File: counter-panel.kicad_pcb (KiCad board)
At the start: 2 copper layers, 60.6 x 133.4 mm, 13 parts

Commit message: Rev. 2
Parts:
- moved REF** 4.90 mm to (124.6, 160.4)
- moved REF** 4.90 mm to (78.6, 160.4)
- moved REF** 4.90 mm to (85.1, 122.2)
- moved REF** 4.90 mm to (101.6, 122.2)
- moved REF** 4.90 mm to (118.1, 122.2)
- moved REF** 4.90 mm to (101.6, 155.0)
- moved REF** 4.90 mm to (101.6, 138.7)
- moved REF** 4.90 mm to (118.1, 138.7)
- moved REF** 4.90 mm to (85.1, 138.7)
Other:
- board size 60.6 x 133.4 mm -> 60.6 x 128.5 mm
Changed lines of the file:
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@@
 	(footprint "MAI_PanelHole:PanelHole_D6Rxx"
 		(layer "F.Cu")
-		(at 118.11 127.095)
+		(at 118.11 122.195)
 		(property "Reference" "REF**"
 			(at 0 -0.5 0)
@@
 		)
 		(attr board_only exclude_from_pos_files exclude_from_bom allow_missing_courtyard)
+		(fp_rect
+			(start -5.65 -6.25)
+			(end 6.25 6.25)
+			(stroke
+				(width 0.05)
+				(type solid)
+			)
+			(fill no)
+			(layer "F.CrtYd")
+		)
 		(fp_text user "${REFERENCE}"
 			(at 0 2.5 0)
@@
 	(footprint "MAI_PanelHole:PanelHole_PJ301BM"
 		(layer "F.Cu")
-		(at 101.6 143.605)
+		(at 101.6 138.705)
 		(property "Reference" "REF**"
 			(at 0 -0.5 0)
@@
 		)
 		(attr board_only exclude_from_pos_files exclude_from_bom allow_missing_courtyard)
+		(fp_rect
+			(start -5.4 -6.2)
+			(end 5.4 5.7)
+			(stroke
+				(width 0.05)
+				(type solid)
+			)
+			(fill no)
+			(layer "F.CrtYd")
+		)
 		(fp_text user "${REFERENCE}"
 			(at 0 2.5 0)
@@
 	(footprint "MAI_Logo:MAI_Logo_10.5mm_Soldermask"
 		(layer "F.Cu")
-		(at 101.6 159.865)
+		(at 101.6 154.965)
 		(property "Reference" "REF**"
 			(at 0 -0.5 0)
@@
 		)
 		(group ""
-			(members "007e59d5-dd87-4414-bfcb-8a791d01e0a8" "5d55bc7f-9524-44fe-8a44-d4192dc5d49f"
-				"ee19ec08-60ec-448d-a128-6061143b3cac"
+			(members "304329a8-93d0-4710-89da-b5f9ca749a7c" "a1dcff84-941b-45ea-a03c-113b23a4899f"
+				"ed1a71e2-07de-497b-ab26-7d1f4ce3553c"
 			)
 		)
@@
 		)
 		(fp_rect
+			(start -2.13 -2.54)
+			(end 17.37 35.56)
+			(stroke
+				(width 0.05)
+				(type solid)
+			)
+			(fill no)
+			(layer "F.CrtYd")
+		)
+		(fp_rect
 			(start 17.12 -2.29)
 			(end -1.88 35.31)
@@
 		)
 		(group ""
-			(members "0314770b-07c4-4799-91cd-ce2d32d9cd09" "46357c1f-7430-4531-8edb-69de8b4cd5fb"
-				"46f7f278-1ce7-49fd-b8e8-32372eb0f30b" "94e10fc9-aa04-4488-8e95-dc1f43b66b6a"
-				"ae31dfa5-9d65-4859-966f-7c5d5160bc3b" "beac1812-f0e9-4054-995f-46d35df900fc"
-				"d999300a-5dc8-4ff8-9753-1f82308b7aea" "df0ef669-530f-4ded-bc9d-675b1c817072"
-				"ebd1850c-bc41-46ad-b8f3-3c44abb019f9"
+			(members "164f0c18-09da-4f02-918c-8de093eaadf8" "17211ef4-0c99-49b5-9bb5-683393077b98"
+				"4afb6f95-e186-4992-9f95-601ac5eb0ac2" "5722b74d-b866-46bd-bd4b-224809068712"
+				"9e1bc70c-4c6f-4915-9856-34eb29197225" "b5a80484-6aaa-4b5e-95ee-2f22a0b5214f"
+				"d0f61f16-cb09-4da3-8dd0-288c4137002b" "d6363b40-4efe-4ee9-a46f-7f5150fb9bf6"
+				"f8c60605-8abd-44bd-bc4b-592a4be05baf"
 			)
 		)
@@
 		)
 		(fp_rect
+			(start -2.13 -2.54)
+			(end 17.37 35.56)
+			(stroke
+				(width 0.05)
+				(type solid)
+			)
+			(fill no)
+			(layer "F.CrtYd")
+		)
+		(fp_rect
 			(start 17.12 -2.29)
 			(end -1.88 35.31)
@@
 		)
 		(group ""
-			(members "0718e5cc-82fb-4867-9d9d-0d31b20be6ac" "0e933451-6ab9-45d7-987d-553bd9a59f48"
-				"39c4f329-30bf-48c5-a186-0e9d4045573b" "40285d72-560b-40a3-becc-59d6b23297b2"
-				"b9054f5f-2db8-4309-b650-e811e8badf08" "be7256dd-f8c9-4556-b094-f6eccc31749b"
-				"c52d14fc-486d-475e-a465-ecf5a4b59eef" "d59265ac-db7d-4d4c-b0e9-78b0ffbd3e86"
-				"f33d80c7-e85c-4af6-96c6-dfac4c1676c2"
+			(members "1924449c-67cb-467a-8796-df98bb2279b6" "3a6cdd18-6018-436c-90c4-f8c9ebc832d7"
+				"4e4a7a91-d7b2-4769-9c2f-26a616b300c3" "72f5ae3b-22af-406f-b730-0e4100dc7158"
+				"c9e218e7-14f0-4782-8d70-630dd5abf210" "d5b6e767-6c86-4224-b7d1-8c03cd33c635"
+				"e360bcd1-de0b-4e42-83ec-22f8f9767f02" "ea660fa0-5717-46c5-b4be-eabed19c45d7"
+				"f14bb1ab-4958-4e47-bdb4-c58802fefbf7"
 			)
 		)
@@
 	(footprint "MAI_PanelHole:PanelHole_D6Rxx"
 		(layer "F.Cu")
-		(at 118.11 143.605)
+		(at 118.11 138.705)
 		(property "Reference" "REF**"
 			(at 0 -0.5 0)
@@
 		)
 		(attr board_only exclude_from_pos_files exclude_from_bom allow_missing_courtyard)
+		(fp_rect
+			(start -5.65 -6.25)
+			(end 6.25 6.25)
+			(stroke
+				(width 0.05)
+				(type solid)
+			)
+			(fill no)
+			(layer "F.CrtYd")
+		)
 		(fp_text user "${REFERENCE}"
 			(at 0 2.5 0)
@@
 	(footprint "MAI_PanelHole:PanelHole_PJ301BM"
 		(layer "F.Cu")
-		(at 85.09 143.605)
+		(at 85.09 138.705)
 		(property "Reference" "REF**"
 			(at 0 -0.5 0)
@@
 		)
 		(attr board_only exclude_from_pos_files exclude_from_bom allow_missing_courtyard)
+		(fp_rect
+			(start -5.4 -6.2)
+			(end 5.4 5.7)
+			(stroke
+				(width 0.05)
+				(type solid)
+			)
+			(fill no)
+			(layer "F.CrtYd")
+		)
 		(fp_text user "${REFERENCE}"
 			(at 0 2.5 0)
@@
 	(footprint "MAI_PanelHole:PanelHole_EurorackMounting"
 		(layer "F.Cu")
-		(at 124.64 165.3)
+		(at 124.64 160.4)
 		(property "Reference" "REF**"
 			(at 0 -0.5 0)
@@
 	(footprint "MAI_PanelHole:PanelHole_EurorackMounting"
 		(layer "F.Cu")
-		(at 78.56 165.3)
+		(at 78.56 160.4)
 		(property "Reference" "REF**"
 			(at 0 -0.5 0)
@@
 	(footprint "MAI_PanelHole:PanelHole_PJ301BM"
 		(layer "F.Cu")
-		(at 85.09 127.095)
+		(at 85.09 122.195)
 		(property "Reference" "REF**"
 			(at 0 -0.5 0)
@@
 		)
 		(attr board_only exclude_from_pos_files exclude_from_bom allow_missing_courtyard)
+		(fp_rect
+			(start -5.4 -6.2)
+			(end 5.4 5.7)
+			(stroke
+				(width 0.05)
+				(type solid)
+			)
+			(fill no)
+			(layer "F.CrtYd")
+		)
 		(fp_text user "${REFERENCE}"
 			(at 0 2.5 0)
@@
 	(footprint "MAI_PanelHole:PanelHole_PJ301BM"
 		(layer "F.Cu")
-		(at 101.6 127.095)
+		(at 101.6 122.195)
 		(property "Reference" "REF**"
 			(at 0 -0.5 0)
@@
 		)
 		(attr board_only exclude_from_pos_files exclude_from_bom allow_missing_courtyard)
+		(fp_rect
+			(start -5.4 -6.2)
+			(end 5.4 5.7)
+			(stroke
+				(width 0.05)
+				(type solid)
+			)
+			(fill no)
+			(layer "F.CrtYd")
+		)
 		(fp_text user "${REFERENCE}"
 			(at 0 2.5 0)
@@
 	)
 	(gr_line
-		(start 90.14 143.605)
-		(end 96.52 143.605)
+		(start 85.09 127.275)
+		(end 85.09 133.625)
+		(stroke
+			(width 0.25)
+			(type solid)
+		)
+		(layer "F.Mask")
+	)
+	(gr_line
+		(start 85.09 133.6675)
+		(end 84.455 133.0325)
+		(stroke
+			(width 0.25)
+			(type solid)
+		)
+		(layer "F.Mask")
+	)
+	(gr_line
+		(start 85.09 133.6675)
+		(end 85.725 133.0325)
+		(stroke
+			(width 0.25)
+			(type solid)
+		)
+		(layer "F.Mask")
+	)
+	(gr_line
+		(start 90.14 122.195)
+		(end 96.52 122.195)
 		(stroke
 			(width 0.25)
@@
 	)
 	(gr_line
-		(start 106.68 127.095)
-		(end 111.76 127.095)
+		(start 90.14 138.705)
+		(end 96.52 138.705)
+		(stroke
+			(width 0.25)
+			(type dash_dot_dot)
+		)
+		(layer "F.Mask")
+	)
+	(gr_line
+		(start 106.68 122.195)
+		(end 111.76 122.195)
 		(stroke
 			(width 0.25)
@@
 	)
 	(gr_line
-		(start 90.14 127.095)
-		(end 96.52 127.095)
-		(stroke
-			(width 0.25)
-			(type dash_dot_dot)
-		)
-		(layer "F.Mask")
-	)
-	(gr_line
-		(start 106.68 143.605)
-		(end 111.76 143.605)
+		(start 106.68 138.705)
+		(end 111.76 138.705)
 		(stroke
 			(width 0.25)
@@
 	(gr_rect
 		(start 71.3 34.9)
-		(end 131.9 168.3)
+		(end 131.9 163.4)
 		(stroke
 			(width 0.05)
@@
 	)
 	(gr_text "Clock In"
-		(at 85.09 121.415 0)
+		(at 85.09 116.515 0)
+		(layer "F.Mask")
+		(effects
+			(font
+				(size 1.6 1.6)
+				(thickness 0.25)
+			)
+			(justify bottom)
+		)
+	)
+	(gr_text "Reset In"
+		(at 101.6 116.515 0)
 		(layer "F.Mask")
 		(effects
@@
 		)
 	)
-	(gr_text "Reset In"
-		(at 101.6 121.415 0)
-		(layer "F.Mask")
-		(effects
-			(font
-				(size 1.6 1.6)
-				(thickness 0.25)
-			)
-			(justify bottom)
-		)
-	)
 	(zone
 		(net 0)
@@
 		(polygon
 			(pts
-				(xy 71.628 35.306) (xy 131.318 35.306) (xy 131.318 167.894) (xy 71.882 167.894)
+				(xy 71.628 35.306) (xy 131.318 35.306) (xy 131.318 162.814) (xy 71.882 162.814)
 			)
 		)
@@
 		(polygon
 			(pts
-				(xy 71.628 35.306) (xy 131.318 35.306) (xy 131.318 167.894) (xy 71.882 167.894)
-			)
-		)
+				(xy 71.628 35.306) (xy 131.318 35.306) (xy 131.318 162.814) (xy 71.882 162.814)
+			)
+		)

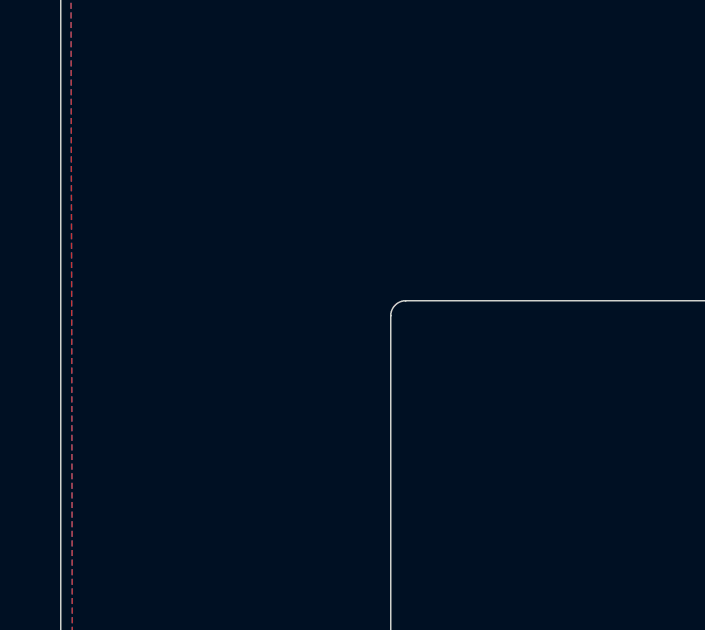
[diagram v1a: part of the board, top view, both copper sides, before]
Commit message: Add pad for standoff to panel
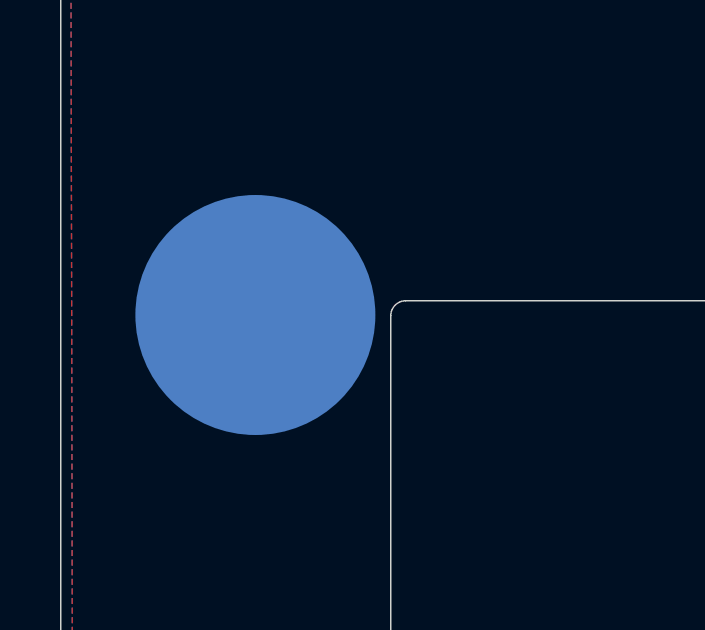
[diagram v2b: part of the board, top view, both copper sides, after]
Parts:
- added REF**: Mounting_Wuerth_WP-SMBU-M4_H7mm_ThreadDepth4mm_NoNPTH_74662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, MAI_Mounting_Wuerth:Mounting_Wuerth_WP-SMBU-M4_H7mm_ThreadDepth4mm_NoNPTH_7466204, B.Cu at (77.8, 53.3)
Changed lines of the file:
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@@
 		(embedded_fonts no)
+	)
+	(footprint "MAI_Mounting_Wuerth:Mounting_Wuerth_WP-SMBU-M4_H7mm_ThreadDepth4mm_NoNPTH_7466204"
+		(layer "B.Cu")
+		(at 77.7875 53.34 180)
+		(property "Reference" "REF**"
+			(at 0 5.5 0)
+			(unlocked yes)
+			(layer "B.SilkS")
+			(hide yes)
+			(effects
+				(font
+					(size 1 1)
+					(thickness 0.1)
+				)
+				(justify mirror)
+			)
+		)
+		(property "Value" "Mounting_Wuerth_WP-SMBU-M4_H7mm_ThreadDepth4mm_NoNPTH_7466204"
+			(at 0 -5 0)
+			(unlocked yes)
+			(layer "B.Fab")
+			(hide yes)
+			(effects
+				(font
+					(size 1 1)
+					(thickness 0.15)
+				)
+				(justify mirror)
+			)
+		)
+		(property "Datasheet" ""
+			(at 0 0 0)
+			(unlocked yes)
+			(layer "B.Fab")
+			(hide yes)
+			(effects
+				(font
+					(size 1 1)
+					(thickness 0.15)
+				)
+				(justify mirror)
+			)
+		)
+		(property "Description" ""
+			(at 0 0 0)
+			(unlocked yes)
+			(layer "B.Fab")
+			(hide yes)
+			(effects
+				(font
+					(size 1 1)
+					(thickness 0.15)
+				)
+				(justify mirror)
+			)
+		)
+		(attr smd)
+		(fp_circle
+			(center 0 0)
+			(end 4.5 0)
+			(stroke
+				(width 0.05)
+				(type solid)
+			)
+			(fill no)
+			(layer "B.CrtYd")
+		)
+		(fp_text user "${REFERENCE}"
+			(at 0 -6.5 0)
+			(unlocked yes)
+			(layer "B.Fab")
+			(effects
+				(font
+					(size 1 1)
+					(thickness 0.15)
+				)
+				(justify mirror)
+			)
+		)
+		(pad "1" smd circle
+			(at 0 0 180)
+			(size 8 8)
+			(layers "B.Cu" "B.Mask" "B.Paste")
+		)
+		(embedded_fonts no)
+		(model "${KIPRJMOD}/kicad-libraries/3dmodels/MAI_Mounting_Wuerth.3dshapes/Mounting_Wuerth_WP-SMBU-M4_H7mm_ThreadDepth4mm_NoNPTH_7466204.stpZ"
+			(offset
+				(xyz 0 0 0)
+			)
+			(scale
+				(xyz 1 1 1)
+			)
+			(rotate
+				(xyz 0 0 0)
+			)
+		)
 	)
 	(gr_line
